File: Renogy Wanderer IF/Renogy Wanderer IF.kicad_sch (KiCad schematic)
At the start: 4 parts

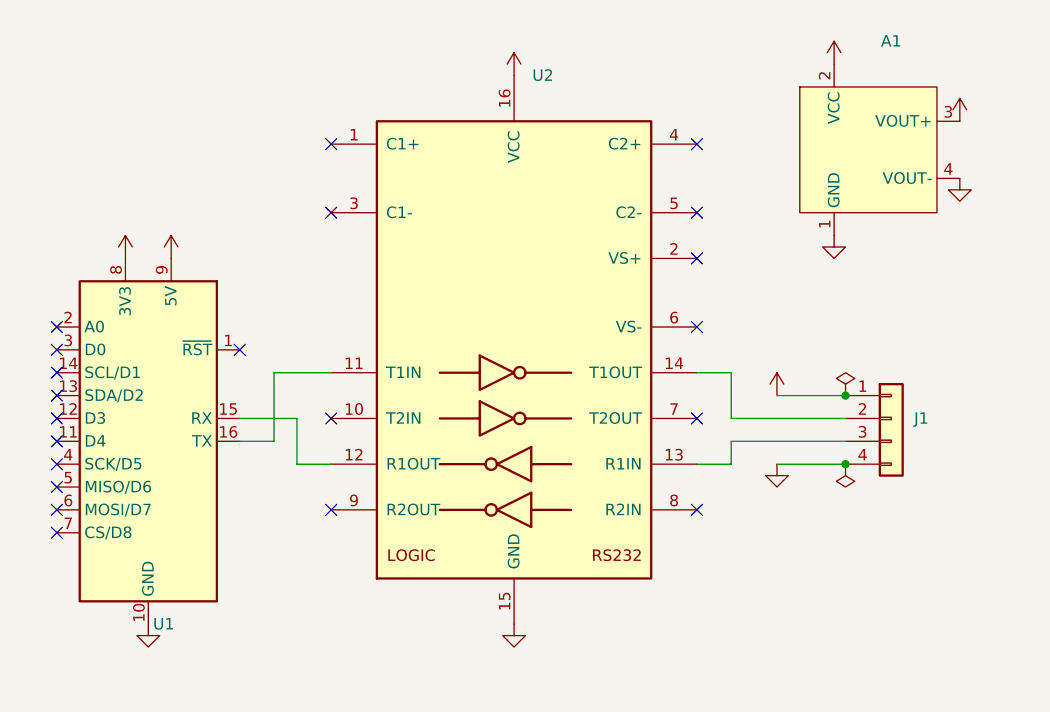
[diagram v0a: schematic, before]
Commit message: Add MAX3232 module
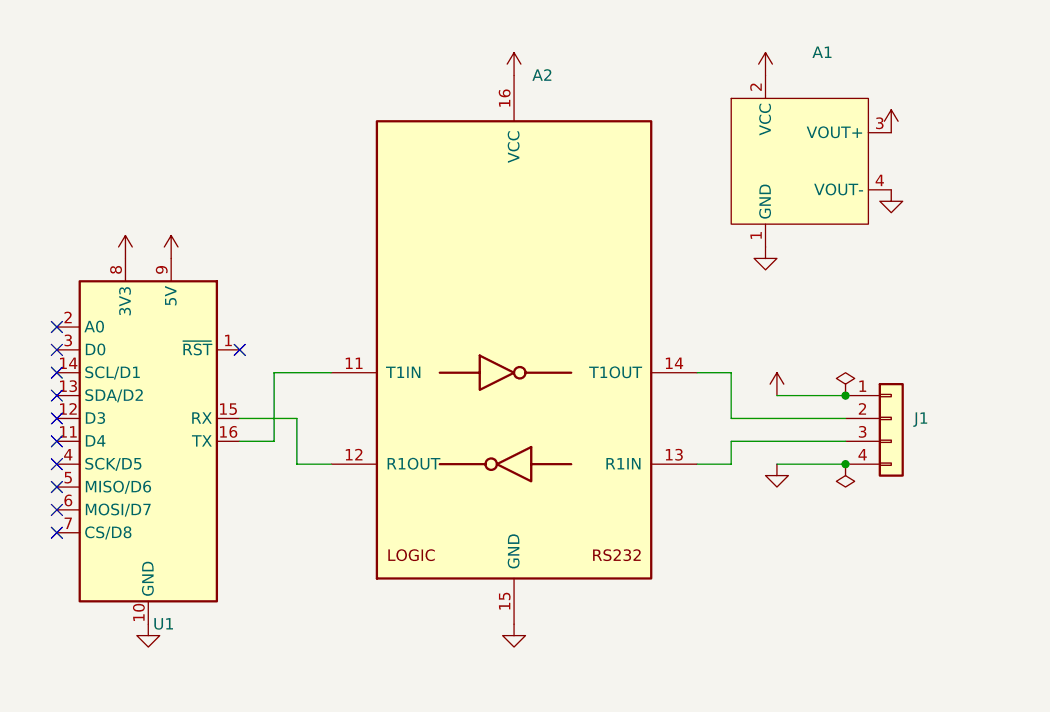
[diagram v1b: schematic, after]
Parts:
- removed U2: (no value), symbol Interface_UART:MAX232
- added A2: (no value), symbol GW_custom:MAX3232 module
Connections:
- net +3V3: now also A2.16 (VCC)
- net GND: now also A2.15 (GND)
- net at U1.15 (RX): now also A2.12 (R1OUT)
- net at U1.16 (TX): now also A2.11 (T1IN)
- net at J1.3 (Pin_3): now also A2.13 (R1IN)
- net at J1.2 (Pin_2): now also A2.14 (T1OUT)
- no-connect marks 21 -> 11
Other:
- moved on the sheet: A1

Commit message: Initial PCB design
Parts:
- removed A1: (no value), symbol GW_custom:MINI-360
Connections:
- net +15V is gone; now on net GND: J1.1 (Pin_1)
- net GND: no longer J1.4 (Pin_4)
- no-connect marks 11 -> 12
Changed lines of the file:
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@@
 (kicad_sch (version 20211123) (generator eeschema)
   (paper "A4")
-  (junction (at 213.36 99.06) (diameter 0) (color 0 0 0 0)
-  )
-  (junction (at 213.36 91.44) (diameter 0) (color 0 0 0 0)
+  (junction (at 135.89 116.84) (diameter 0) (color 0 0 0 0)
+  )
+  (junction (at 138.43 76.2) (diameter 0) (color 0 0 0 0)
   )
   (no_connect (at 125.73 83.82))
@@
   (no_connect (at 125.73 99.06))
   (no_connect (at 125.73 104.14))
+  (no_connect (at 213.36 99.06))
   (no_connect (at 125.73 86.36))
   (wire (pts (xy 200.66 93.98) (xy 213.36 93.98))
@@
     (stroke (width 0) (type default) (color 0 0 0 0))
   )
+  (wire (pts (xy 127 116.84) (xy 135.89 116.84))
+    (stroke (width 0) (type default) (color 0 0 0 0))
+  )
+  (wire (pts (xy 127 118.11) (xy 127 116.84))
+    (stroke (width 0) (type default) (color 0 0 0 0))
+  )
   (wire (pts (xy 156.21 99.06) (xy 152.4 99.06))
     (stroke (width 0) (type default) (color 0 0 0 0))
   )
-  (wire (pts (xy 205.74 91.44) (xy 213.36 91.44))
-    (stroke (width 0) (type default) (color 0 0 0 0))
-  )
   (wire (pts (xy 152.4 99.06) (xy 152.4 93.98))
     (stroke (width 0) (type default) (color 0 0 0 0))
   )
-  (wire (pts (xy 205.74 99.06) (xy 213.36 99.06))
-    (stroke (width 0) (type default) (color 0 0 0 0))
-  )
   (wire (pts (xy 200.66 96.52) (xy 213.36 96.52))
     (stroke (width 0) (type default) (color 0 0 0 0))
@@
     (stroke (width 0) (type default) (color 0 0 0 0))
   )
+  (wire (pts (xy 213.36 85.09) (xy 207.01 85.09))
+    (stroke (width 0) (type default) (color 0 0 0 0))
+  )
+  (wire (pts (xy 213.36 91.44) (xy 213.36 85.09))
+    (stroke (width 0) (type default) (color 0 0 0 0))
+  )
   (wire (pts (xy 200.66 88.9) (xy 200.66 93.98))
     (stroke (width 0) (type default) (color 0 0 0 0))
   )
+  (wire (pts (xy 138.43 76.2) (xy 146.05 76.2))
+    (stroke (width 0) (type default) (color 0 0 0 0))
+  )
   (wire (pts (xy 196.85 99.06) (xy 200.66 99.06))
     (stroke (width 0) (type default) (color 0 0 0 0))
@@
   (wire (pts (xy 156.21 88.9) (xy 149.86 88.9))
     (stroke (width 0) (type default) (color 0 0 0 0))
-  )
-  (symbol (lib_id "power:GND") (at 218.44 68.58 0) (unit 1)
-    (in_bom yes) (on_board yes) (fields_autoplaced)
-    (property "Reference" "#PWR010" (id 0) (at 218.44 74.93 0)
-      (effects (font (size 1.27 1.27)) hide)
-    )
-    (property "Value" "" (id 1) (at 218.44 73.66 0))
-    (property "Footprint" "" (id 2) (at 218.44 68.58 0)
-      (effects (font (size 1.27 1.27)) hide)
-    )
-    (property "Datasheet" "" (id 3) (at 218.44 68.58 0)
-      (effects (font (size 1.27 1.27)) hide)
-    )
-    (pin "1")
   )
   (symbol (lib_id "power:+3.3V") (at 133.35 76.2 0) (unit 1)
@@
     (pin "1")
   )
-  (symbol (lib_id "power:GND") (at 204.47 74.93 0) (unit 1)
-    (in_bom yes) (on_board yes) (fields_autoplaced)
-    (property "Reference" "#PWR06" (id 0) (at 204.47 81.28 0)
-      (effects (font (size 1.27 1.27)) hide)
-    )
-    (property "Value" "" (id 1) (at 204.47 80.01 0))
-    (property "Footprint" "" (id 2) (at 204.47 74.93 0)
-      (effects (font (size 1.27 1.27)) hide)
-    )
-    (property "Datasheet" "" (id 3) (at 204.47 74.93 0)
-      (effects (font (size 1.27 1.27)) hide)
-    )
-    (pin "1")
-  )
-  (symbol (lib_id "power:+5V") (at 218.44 62.23 0) (unit 1)
-    (in_bom yes) (on_board yes) (fields_autoplaced)
-    (property "Reference" "#PWR011" (id 0) (at 218.44 66.04 0)
-      (effects (font (size 1.27 1.27)) hide)
-    )
-    (property "Value" "" (id 1) (at 218.44 57.15 0))
-    (property "Footprint" "" (id 2) (at 218.44 62.23 0)
-      (effects (font (size 1.27 1.27)) hide)
-    )
-    (property "Datasheet" "" (id 3) (at 218.44 62.23 0)
-      (effects (font (size 1.27 1.27)) hide)
-    )
-    (pin "1")
-  )
-  (symbol (lib_id "power:PWR_FLAG") (at 213.36 91.44 0) (unit 1)
-    (in_bom yes) (on_board yes) (fields_autoplaced)
-    (property "Reference" "#FLG02" (id 0) (at 213.36 89.535 0)
-      (effects (font (size 1.27 1.27)) hide)
-    )
-    (property "Value" "" (id 1) (at 213.36 86.36 0))
-    (property "Footprint" "" (id 2) (at 213.36 91.44 0)
-      (effects (font (size 1.27 1.27)) hide)
-    )
-    (property "Datasheet" "~" (id 3) (at 213.36 91.44 0)
-      (effects (font (size 1.27 1.27)) hide)
-    )
-    (pin "1")
-  )
-  (symbol (lib_id "GW_custom:MINI-360") (at 205.74 55.88 0) (unit 1)
-    (in_bom yes) (on_board yes)
-    (property "Reference" "A1" (id 0) (at 210.82 53.34 0))
-    (property "Value" "" (id 1) (at 210.82 55.88 0))
-    (property "Footprint" "" (id 2) (at 205.74 55.88 0)
-      (effects (font (size 1.27 1.27)) hide)
-    )
-    (property "Datasheet" "" (id 3) (at 205.74 55.88 0)
-      (effects (font (size 1.27 1.27)) hide)
-    )
-    (pin "1")
-    (pin "2")
-    (pin "3")
-    (pin "4")
+  (symbol (lib_id "power:PWR_FLAG") (at 146.05 76.2 0) (unit 1)
+    (in_bom yes) (on_board yes) (fields_autoplaced)
+    (property "Reference" "#FLG02" (id 0) (at 146.05 74.295 0)
+      (effects (font (size 1.27 1.27)) hide)
+    )
+    (property "Value" "" (id 1) (at 146.05 71.12 0))
+    (property "Footprint" "" (id 2) (at 146.05 76.2 0)
+      (effects (font (size 1.27 1.27)) hide)
+    )
+    (property "Datasheet" "~" (id 3) (at 146.05 76.2 0)
+      (effects (font (size 1.27 1.27)) hide)
+    )
+    (pin "1")
   )
   (symbol (lib_id "MCU_Module:WeMos_D1_mini") (at 135.89 96.52 0) (mirror y) (unit 1)
@@
     (pin "9")
   )
-  (symbol (lib_id "power:+15V") (at 204.47 55.88 0) (unit 1)
-    (in_bom yes) (on_board yes) (fields_autoplaced)
-    (property "Reference" "#PWR07" (id 0) (at 204.47 59.69 0)
-      (effects (font (size 1.27 1.27)) hide)
-    )
-    (property "Value" "" (id 1) (at 204.47 50.8 0))
-    (property "Footprint" "" (id 2) (at 204.47 55.88 0)
-      (effects (font (size 1.27 1.27)) hide)
-    )
-    (property "Datasheet" "" (id 3) (at 204.47 55.88 0)
-      (effects (font (size 1.27 1.27)) hide)
-    )
-    (pin "1")
-  )
-  (symbol (lib_id "power:GND") (at 205.74 99.06 0) (unit 1)
-    (in_bom yes) (on_board yes) (fields_autoplaced)
-    (property "Reference" "#PWR03" (id 0) (at 205.74 105.41 0)
-      (effects (font (size 1.27 1.27)) hide)
-    )
-    (property "Value" "" (id 1) (at 205.74 104.14 0))
-    (property "Footprint" "" (id 2) (at 205.74 99.06 0)
-      (effects (font (size 1.27 1.27)) hide)
-    )
-    (property "Datasheet" "" (id 3) (at 205.74 99.06 0)
+  (symbol (lib_id "power:GND") (at 207.01 85.09 0) (unit 1)
+    (in_bom yes) (on_board yes) (fields_autoplaced)
+    (property "Reference" "#PWR03" (id 0) (at 207.01 91.44 0)
+      (effects (font (size 1.27 1.27)) hide)
+    )
+    (property "Value" "" (id 1) (at 207.01 90.17 0))
+    (property "Footprint" "" (id 2) (at 207.01 85.09 0)
+      (effects (font (size 1.27 1.27)) hide)
+    )
+    (property "Datasheet" "" (id 3) (at 207.01 85.09 0)
       (effects (font (size 1.27 1.27)) hide)
     )
@@
     )
     (property "Datasheet" "" (id 3) (at 138.43 76.2 0)
-      (effects (font (size 1.27 1.27)) hide)
-    )
-    (pin "1")
-  )
-  (symbol (lib_id "power:+15V") (at 205.74 91.44 0) (unit 1)
-    (in_bom yes) (on_board yes) (fields_autoplaced)
-    (property "Reference" "#PWR08" (id 0) (at 205.74 95.25 0)
-      (effects (font (size 1.27 1.27)) hide)
-    )
-    (property "Value" "" (id 1) (at 205.74 86.36 0))
-    (property "Footprint" "" (id 2) (at 205.74 91.44 0)
-      (effects (font (size 1.27 1.27)) hide)
-    )
-    (property "Datasheet" "" (id 3) (at 205.74 91.44 0)
       (effects (font (size 1.27 1.27)) hide)
     )
@@
     (pin "1")
   )
-  (symbol (lib_id "power:PWR_FLAG") (at 213.36 99.06 0) (mirror x) (unit 1)
-    (in_bom yes) (on_board yes) (fields_autoplaced)
-    (property "Reference" "#FLG01" (id 0) (at 213.36 100.965 0)
-      (effects (font (size 1.27 1.27)) hide)
-    )
-    (property "Value" "" (id 1) (at 213.36 104.14 0))
-    (property "Footprint" "" (id 2) (at 213.36 99.06 0)
-      (effects (font (size 1.27 1.27)) hide)
-    )
-    (property "Datasheet" "~" (id 3) (at 213.36 99.06 0)
+  (symbol (lib_id "power:PWR_FLAG") (at 127 118.11 0) (mirror x) (unit 1)
+    (in_bom yes) (on_board yes) (fields_autoplaced)
+    (property "Reference" "#FLG01" (id 0) (at 127 120.015 0)
+      (effects (font (size 1.27 1.27)) hide)
+    )
+    (property "Value" "" (id 1) (at 127 123.19 0))
+    (property "Footprint" "" (id 2) (at 127 118.11 0)
+      (effects (font (size 1.27 1.27)) hide)
+    )
+    (property "Datasheet" "~" (id 3) (at 127 118.11 0)
       (effects (font (size 1.27 1.27)) hide)
     )
@@
       (reference "#PWR05") (unit 1) (value "+5V") (footprint "")
     )
-    (path "/1f1fd397-0f7e-44c2-9400-f845137b03cb"
-      (reference "#PWR06") (unit 1) (value "GND") (footprint "")
-    )
-    (path "/6f7fcd89-2d4e-4d91-9ef8-38705a09ac39"
-      (reference "#PWR07") (unit 1) (value "+15V") (footprint "")
-    )
-    (path "/d3453189-eae1-425b-bc82-f31d064a13f1"
-      (reference "#PWR08") (unit 1) (value "+15V") (footprint "")
-    )
     (path "/dae4dc93-ed60-4243-aca2-ac7b7eb6d735"
       (reference "#PWR09") (unit 1) (value "+3.3V") (footprint "")
     )
-    (path "/059640c8-37a2-47f1-a560-f9576acb0bc6"
-      (reference "#PWR010") (unit 1) (value "GND") (footprint "")
-    )
-    (path "/3edd5868-1d49-42c5-8211-f6a4af98495b"
-      (reference "#PWR011") (unit 1) (value "+5V") (footprint "")
-    )
-    (path "/51978987-bee1-4381-9232-b8b6e9a5316d"
-      (reference "A1") (unit 1) (value "MINI-360") (footprint "Module:MINI-360")
-    )
     (path "/da01b3e4-26f2-4f90-b4fe-3db1c5dc3840"
